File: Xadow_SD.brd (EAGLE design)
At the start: 25.5 x 20.4 mm, 6 parts, among them IC1 4050D, J1 MICRO-SDCARD-CONNECTOR-330006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, J2 12p FPC bottom contact, J3 12p FPC bottom contact

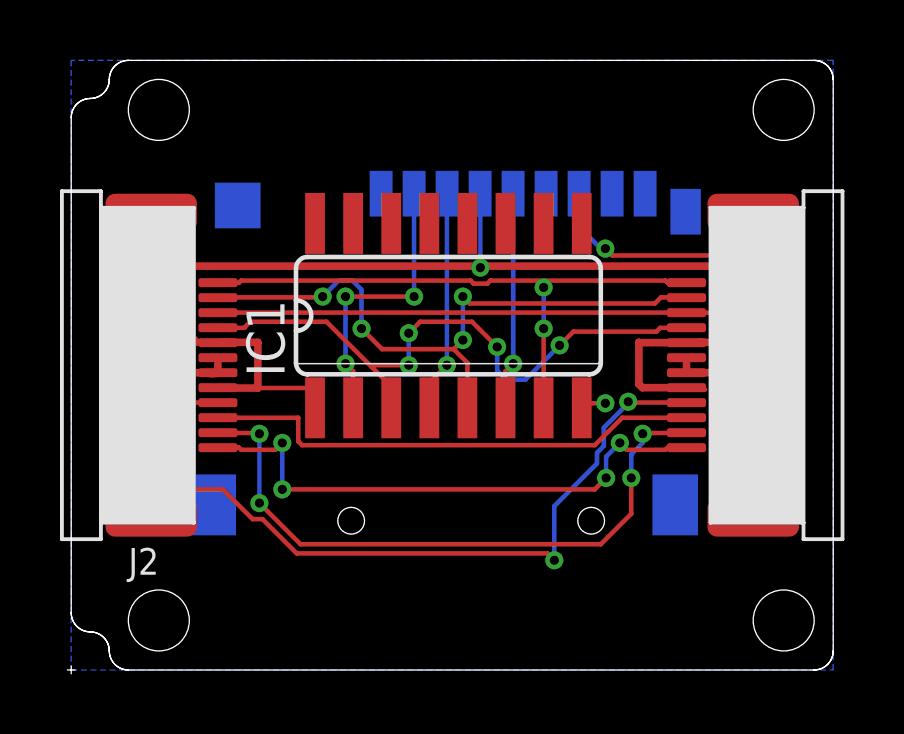
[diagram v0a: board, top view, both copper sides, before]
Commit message: Add 6-pin header
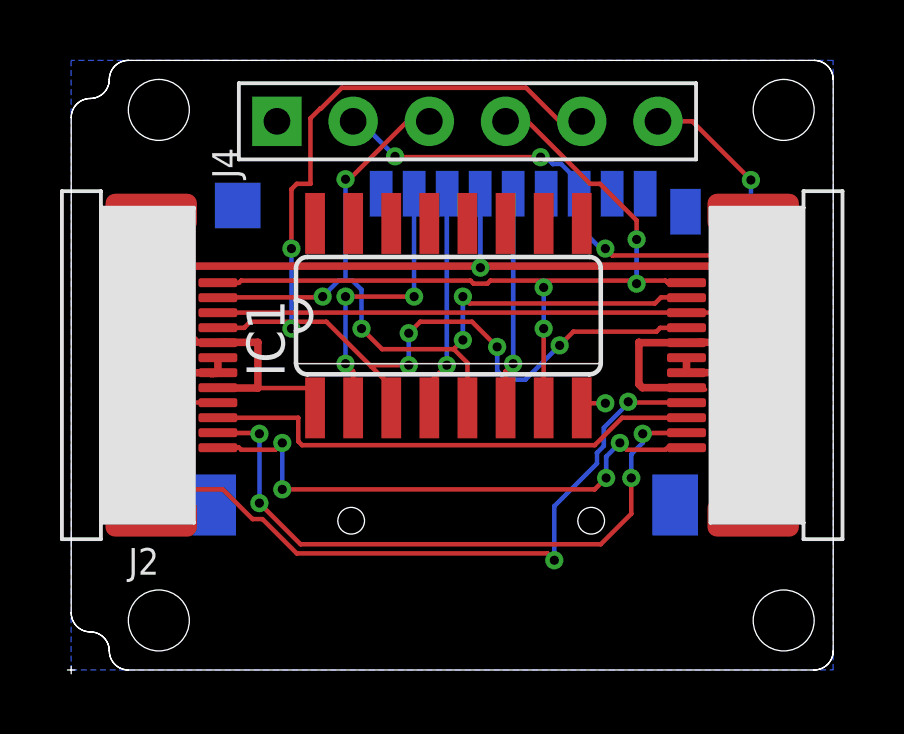
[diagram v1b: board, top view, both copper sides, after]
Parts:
- added J4: CONNECTOR-HEADER-6P-3460650P1, OPL:1X6P-2.54-2.54-11.6-3.0-BLACK-MALE
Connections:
- net 3V3: now also J4.6
- net GND: now also J1.G1, J1.G2, J1.G3, J1.G4, J4.1
- net PB1/D15/SCK: now also J4.4
- net PB2/D16/MOSI: now also J4.3
- net PB3/D14/MISO: now also J4.2
- net PF0/A5: now also J4.5
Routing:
- net PF0/A5: track 21.2 -> 38.9 mm, vias 4 -> 6
- net PB3/D14/MISO: track 25.0 -> 34.1 mm, vias 3 -> 5
- net PB1/D15/SCK: track 20.0 -> 28.0 mm, vias 2 -> 4
- net 3V3: track 42.2 -> 49.2 mm, vias 1 -> 3
- net PB2/D16/MOSI: track 21.5 -> 28.4 mm, vias 4 -> 5
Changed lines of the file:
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@@
 <layer number="18" name="Vias" color="2" fill="1" visible="yes" active="yes"/>
 <layer number="19" name="Unrouted" color="6" fill="1" visible="yes" active="yes"/>
-<layer number="20" name="Dimension" color="5" fill="1" visible="no" active="yes"/>
+<layer number="20" name="Dimension" color="5" fill="1" visible="yes" active="yes"/>
 <layer number="21" name="tPlace" color="7" fill="1" visible="no" active="yes"/>
 <layer number="22" name="bPlace" color="3" fill="1" visible="no" active="yes"/>
-<layer number="23" name="tOrigins" color="15" fill="1" visible="no" active="yes"/>
-<layer number="24" name="bOrigins" color="3" fill="1" visible="no" active="yes"/>
+<layer number="23" name="tOrigins" color="15" fill="1" visible="yes" active="yes"/>
+<layer number="24" name="bOrigins" color="3" fill="1" visible="yes" active="yes"/>
 <layer number="25" name="tNames" color="7" fill="1" visible="no" active="yes"/>
 <layer number="26" name="bNames" color="3" fill="1" visible="no" active="yes"/>
@@
 <element name="IC1" library="40xx" package="SO16" value="4050D" x="20.447" y="18.161"/>
 <element name="J1" library="OPL" package="9P-SMD-W-RING" value="MICRO-SDCARD-CONNECTOR-3300060P1" x="20.32" y="14.732" rot="MR270"/>
+<element name="J4" library="OPL" package="1X6P-2.54-2.54-11.6-3.0-BLACK-MALE" value="CONNECTOR-HEADER-6P-3460650P1" x="21.082" y="24.638" rot="R90"/>
 </elements>
 <signals>
@@
 <wire x1="12.7" y1="17.272" x2="12.764" y2="17.26" width="0.1524" layer="1"/>
 <via x="21.5138" y="19.7612" extent="1-16" drill="0.3048"/>
+<contactref element="J4" pad="6"/>
+<wire x1="28.575" y1="24.638" x2="27.432" y2="24.638" width="0.1524" layer="1"/>
+<wire x1="30.5308" y1="22.6822" x2="28.575" y2="24.638" width="0.1524" layer="1"/>
+<wire x1="30.5308" y1="20.3962" x2="30.5308" y2="22.6822" width="0.1524" layer="16"/>
+<wire x1="30.0482" y1="19.9136" x2="30.5308" y2="20.3962" width="0.1524" layer="1"/>
+<wire x1="30.0482" y1="19.9136" x2="29.972" y2="19.812" width="0.1524" layer="1"/>
+<via x="30.5308" y="22.6822" extent="1-16" drill="0.3048"/>
+<via x="30.5308" y="20.3962" extent="1-16" drill="0.3048"/>
 </signal>
 <signal name="GND">
@@
 <wire x1="12.764" y1="16.76" x2="12.764" y2="16.26" width="0.254" layer="1"/>
 <wire x1="12.4206" y1="16.256" x2="9.525" y2="16.256" width="0.254" layer="1"/>
+<contactref element="J4" pad="1"/>
+<contactref element="J1" pad="G3"/>
+<contactref element="J1" pad="G2"/>
+<contactref element="J1" pad="G1"/>
+<contactref element="J1" pad="G4"/>
 </signal>
 <signal name="PB1/D15/SCK">
@@
 <wire x1="21.7424" y1="19.2278" x2="21.2852" y2="19.2278" width="0.1524" layer="1"/>
 <wire x1="21.844" y1="19.3294" x2="21.7424" y2="19.2278" width="0.1524" layer="1"/>
-<wire x1="27.686" y1="19.3294" x2="23.622" y2="19.3294" width="0.1524" layer="1"/>
+<wire x1="27.686" y1="19.3294" x2="26.7208" y2="19.3294" width="0.1524" layer="1"/>
+<wire x1="26.7208" y1="19.3294" x2="23.622" y2="19.3294" width="0.1524" layer="1"/>
 <wire x1="23.622" y1="19.3294" x2="21.844" y2="19.3294" width="0.1524" layer="1"/>
 <wire x1="27.7622" y1="19.2532" x2="27.686" y2="19.3294" width="0.1524" layer="1"/>
@@
 <via x="23.622" y="17.7292" extent="1-16" drill="0.3048"/>
 <via x="23.622" y="19.1008" extent="1-16" drill="0.3048"/>
+<contactref element="J4" pad="4"/>
+<wire x1="23.0886" y1="24.638" x2="22.352" y2="24.638" width="0.1524" layer="1"/>
+<wire x1="25.1714" y1="22.5552" x2="23.0886" y2="24.638" width="0.1524" layer="1"/>
+<wire x1="25.5016" y1="22.5552" x2="25.1714" y2="22.5552" width="0.1524" layer="1"/>
+<wire x1="26.7208" y1="21.336" x2="25.5016" y2="22.5552" width="0.1524" layer="1"/>
+<wire x1="26.7208" y1="20.701" x2="26.7208" y2="21.336" width="0.1524" layer="1"/>
+<wire x1="26.7208" y1="19.2278" x2="26.7208" y2="20.701" width="0.1524" layer="16"/>
+<wire x1="26.7208" y1="19.2278" x2="26.7208" y2="19.3294" width="0.1524" layer="1"/>
+<via x="26.7208" y="20.701" extent="1-16" drill="0.3048"/>
+<via x="26.7208" y="19.2278" extent="1-16" drill="0.3048"/>
 </signal>
 <signal name="PB3/D14/MISO">
@@
 <via x="29.5148" y="20.3962" extent="1-16" drill="0.3048"/>
 <via x="29.5148" y="18.5166" extent="1-16" drill="0.3048"/>
+<contactref element="J4" pad="2"/>
+<wire x1="17.272" y1="24.3078" x2="17.272" y2="24.638" width="0.1524" layer="16"/>
+<wire x1="17.3482" y1="24.2316" x2="17.272" y2="24.3078" width="0.1524" layer="16"/>
+<wire x1="17.907" y1="24.2316" x2="17.3482" y2="24.2316" width="0.1524" layer="16"/>
+<wire x1="18.669" y1="23.4696" x2="17.907" y2="24.2316" width="0.1524" layer="16"/>
+<wire x1="18.6944" y1="23.4442" x2="18.669" y2="23.4696" width="0.1524" layer="1"/>
+<wire x1="23.5204" y1="23.4442" x2="18.6944" y2="23.4442" width="0.1524" layer="1"/>
+<wire x1="23.6982" y1="23.4442" x2="23.5204" y2="23.4442" width="0.1524" layer="16"/>
+<wire x1="23.9268" y1="23.2156" x2="23.6982" y2="23.4442" width="0.1524" layer="16"/>
+<wire x1="24.2062" y1="23.2156" x2="23.9268" y2="23.2156" width="0.1524" layer="16"/>
+<wire x1="24.638" y1="22.7838" x2="24.2062" y2="23.2156" width="0.1524" layer="16"/>
+<wire x1="24.8158" y1="22.7838" x2="24.638" y2="22.7838" width="0.1524" layer="16"/>
+<wire x1="24.8158" y1="22.2758" x2="24.8158" y2="22.7838" width="0.1524" layer="16"/>
+<wire x1="24.8158" y1="22.2758" x2="24.806" y2="22.225" width="0.1524" layer="16"/>
+<via x="18.669" y="23.4696" extent="1-16" drill="0.3048"/>
+<via x="23.5204" y="23.4442" extent="1-16" drill="0.3048"/>
 </signal>
 <signal name="PB2/D16/MOSI">
@@
 <wire x1="16.256" y1="18.796" x2="16.2306" y2="18.7706" width="0.1524" layer="1"/>
 <wire x1="16.7894" y1="19.3294" x2="16.256" y2="18.796" width="0.1524" layer="16"/>
-<wire x1="17.2466" y1="19.3294" x2="16.7894" y2="19.3294" width="0.1524" layer="16"/>
+<wire x1="17.2466" y1="19.3294" x2="17.018" y2="19.3294" width="0.1524" layer="16"/>
+<wire x1="17.018" y1="19.3294" x2="16.7894" y2="19.3294" width="0.1524" layer="16"/>
 <wire x1="17.5514" y1="19.0246" x2="17.2466" y2="19.3294" width="0.1524" layer="16"/>
 <wire x1="17.5514" y1="17.7292" x2="17.5514" y2="19.0246" width="0.1524" layer="16"/>
@@
 <via x="20.9296" y="18.796" extent="1-16" drill="0.3048"/>
 <via x="20.9296" y="17.3482" extent="1-16" drill="0.3048"/>
+<contactref element="J4" pad="3"/>
+<wire x1="19.0754" y1="24.638" x2="19.812" y2="24.638" width="0.1524" layer="1"/>
+<wire x1="17.145" y1="22.7076" x2="19.0754" y2="24.638" width="0.1524" layer="1"/>
+<wire x1="17.018" y1="22.7076" x2="17.145" y2="22.7076" width="0.1524" layer="1"/>
+<wire x1="17.018" y1="19.3294" x2="17.018" y2="22.7076" width="0.1524" layer="16"/>
+<via x="17.018" y="22.7076" extent="1-16" drill="0.3048"/>
 </signal>
 <signal name="PD3/TXO/D1">
@@
 <wire x1="13.6398" y1="17.7546" x2="12.8524" y2="17.7546" width="0.1524" layer="1"/>
 <wire x1="13.843" y1="17.9578" x2="13.6398" y2="17.7546" width="0.1524" layer="1"/>
-<wire x1="16.383" y1="17.9578" x2="13.843" y2="17.9578" width="0.1524" layer="1"/>
+<wire x1="16.383" y1="17.9578" x2="15.2146" y2="17.9578" width="0.1524" layer="1"/>
+<wire x1="15.2146" y1="17.9578" x2="13.843" y2="17.9578" width="0.1524" layer="1"/>
 <wire x1="18.542" y1="15.7988" x2="17.8816" y2="16.4592" width="0.1524" layer="1"/>
 <wire x1="17.8816" y1="16.4592" x2="16.383" y2="17.9578" width="0.1524" layer="1"/>
@@
 <via x="19.1262" y="17.5768" extent="1-16" drill="0.3048"/>
 <via x="19.1262" y="16.51" extent="1-16" drill="0.3048"/>
+<contactref element="J4" pad="5"/>
+<wire x1="24.1554" y1="24.638" x2="24.892" y2="24.638" width="0.1524" layer="1"/>
+<wire x1="23.0378" y1="25.7556" x2="24.1554" y2="24.638" width="0.1524" layer="1"/>
+<wire x1="16.891" y1="25.7556" x2="23.0378" y2="25.7556" width="0.1524" layer="1"/>
+<wire x1="16.2052" y1="25.0698" x2="16.891" y2="25.7556" width="0.1524" layer="1"/>
+<wire x1="16.1798" y1="25.0698" x2="16.2052" y2="25.0698" width="0.1524" layer="1"/>
+<wire x1="15.8496" y1="24.7396" x2="16.1798" y2="25.0698" width="0.1524" layer="1"/>
+<wire x1="15.8496" y1="22.5552" x2="15.8496" y2="24.7396" width="0.1524" layer="1"/>
+<wire x1="15.3924" y1="22.5552" x2="15.8496" y2="22.5552" width="0.1524" layer="1"/>
+<wire x1="15.2146" y1="22.3774" x2="15.3924" y2="22.5552" width="0.1524" layer="1"/>
+<wire x1="15.2146" y1="20.3962" x2="15.2146" y2="22.3774" width="0.1524" layer="1"/>
+<wire x1="15.2146" y1="17.7292" x2="15.2146" y2="20.3962" width="0.1524" layer="16"/>
+<wire x1="15.2146" y1="17.9578" x2="15.2146" y2="17.7292" width="0.1524" layer="1"/>
+<via x="15.2146" y="20.3962" extent="1-16" drill="0.3048"/>
+<via x="15.2146" y="17.7292" extent="1-16" drill="0.3048"/>
 </signal>
 <signal name="PD1/SDA/D2">

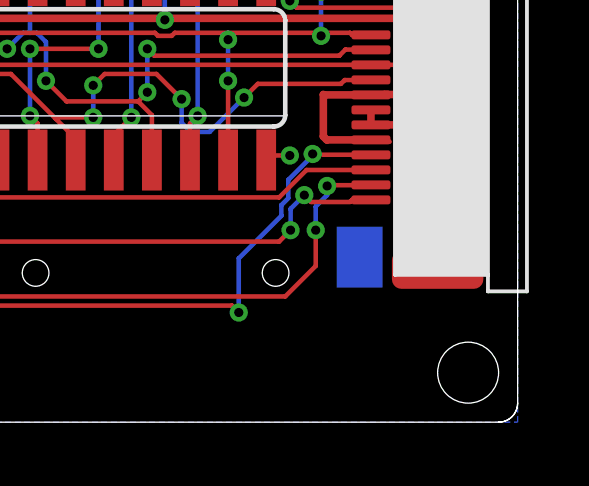
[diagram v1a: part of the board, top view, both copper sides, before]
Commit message: Add labels and move graphics
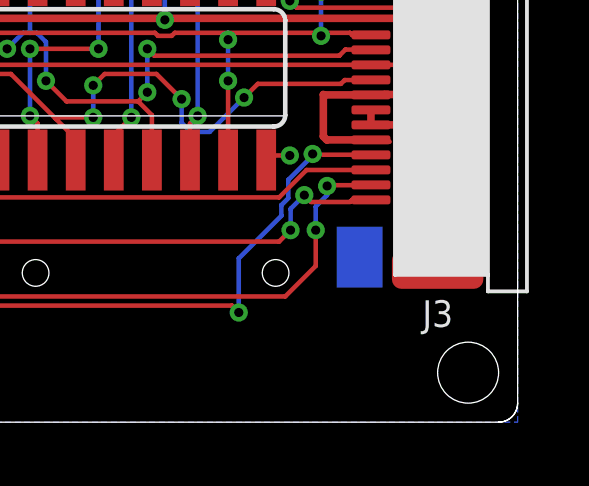
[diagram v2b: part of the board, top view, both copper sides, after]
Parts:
- moved U$2 15.4 mm to (31.1, 12.7), turned to 270 degrees
- moved U$3 7.94 mm to (33.0, 22.9), turned to 270 degrees
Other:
- board text added: "3V3"
- board text added: "CS"
- board text added: "GND"
- board text added: "MISO"
- board text added: "MOSI"
- board text added: "SCK"
- board text added: "by Tisham Dhar"
- board text added: "v2.0 02/09/2014"
- board text removed: "by Seeed Studio"
- board text removed: "v1.0 06/08/2014"
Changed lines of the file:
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@@
 <layer number="19" name="Unrouted" color="6" fill="1" visible="yes" active="yes"/>
 <layer number="20" name="Dimension" color="5" fill="1" visible="yes" active="yes"/>
-<layer number="21" name="tPlace" color="7" fill="1" visible="no" active="yes"/>
-<layer number="22" name="bPlace" color="3" fill="1" visible="no" active="yes"/>
+<layer number="21" name="tPlace" color="7" fill="1" visible="yes" active="yes"/>
+<layer number="22" name="bPlace" color="3" fill="1" visible="yes" active="yes"/>
 <layer number="23" name="tOrigins" color="15" fill="1" visible="yes" active="yes"/>
 <layer number="24" name="bOrigins" color="3" fill="1" visible="yes" active="yes"/>
-<layer number="25" name="tNames" color="7" fill="1" visible="no" active="yes"/>
-<layer number="26" name="bNames" color="3" fill="1" visible="no" active="yes"/>
-<layer number="27" name="tValues" color="7" fill="1" visible="no" active="yes"/>
-<layer number="28" name="bValues" color="7" fill="1" visible="no" active="yes"/>
-<layer number="29" name="tStop" color="7" fill="3" visible="no" active="yes"/>
-<layer number="30" name="bStop" color="3" fill="6" visible="no" active="yes"/>
-<layer number="31" name="tCream" color="7" fill="4" visible="no" active="yes"/>
-<layer number="32" name="bCream" color="3" fill="5" visible="no" active="yes"/>
-<layer number="33" name="tFinish" color="6" fill="3" visible="no" active="yes"/>
-<layer number="34" name="bFinish" color="3" fill="6" visible="no" active="yes"/>
-<layer number="35" name="tGlue" color="7" fill="4" visible="no" active="yes"/>
-<layer number="36" name="bGlue" color="3" fill="5" visible="no" active="yes"/>
-<layer number="37" name="tTest" color="7" fill="1" visible="no" active="yes"/>
-<layer number="38" name="bTest" color="3" fill="1" visible="no" active="yes"/>
-<layer number="39" name="tKeepout" color="4" fill="11" visible="no" active="yes"/>
-<layer number="40" name="bKeepout" color="1" fill="11" visible="no" active="yes"/>
-<layer number="41" name="tRestrict" color="4" fill="10" visible="no" active="yes"/>
-<layer number="42" name="bRestrict" color="1" fill="10" visible="no" active="yes"/>
-<layer number="43" name="vRestrict" color="2" fill="10" visible="no" active="yes"/>
-<layer number="44" name="Drills" color="7" fill="1" visible="no" active="yes"/>
-<layer number="45" name="Holes" color="7" fill="1" visible="no" active="yes"/>
-<layer number="46" name="Milling" color="3" fill="1" visible="no" active="yes"/>
-<layer number="47" name="Measures" color="7" fill="1" visible="no" active="yes"/>
-<layer number="48" name="Document" color="7" fill="1" visible="no" active="yes"/>
-<layer number="49" name="Reference" color="7" fill="1" visible="no" active="yes"/>
-<layer number="50" name="dxf" color="7" fill="1" visible="no" active="yes"/>
-<layer number="51" name="tDocu" color="7" fill="1" visible="no" active="yes"/>
-<layer number="52" name="bDocu" color="7" fill="1" visible="no" active="yes"/>
+<layer number="25" name="tNames" color="7" fill="1" visible="yes" active="yes"/>
+<layer number="26" name="bNames" color="3" fill="1" visible="yes" active="yes"/>
+<layer number="27" name="tValues" color="7" fill="1" visible="yes" active="yes"/>
+<layer number="28" name="bValues" color="7" fill="1" visible="yes" active="yes"/>
+<layer number="29" name="tStop" color="7" fill="3" visible="yes" active="yes"/>
+<layer number="30" name="bStop" color="3" fill="6" visible="yes" active="yes"/>
+<layer number="31" name="tCream" color="7" fill="4" visible="yes" active="yes"/>
+<layer number="32" name="bCream" color="3" fill="5" visible="yes" active="yes"/>
+<layer number="33" name="tFinish" color="6" fill="3" visible="yes" active="yes"/>
+<layer number="34" name="bFinish" color="3" fill="6" visible="yes" active="yes"/>
+<layer number="35" name="tGlue" color="7" fill="4" visible="yes" active="yes"/>
+<layer number="36" name="bGlue" color="3" fill="5" visible="yes" active="yes"/>
+<layer number="37" name="tTest" color="7" fill="1" visible="yes" active="yes"/>
+<layer number="38" name="bTest" color="3" fill="1" visible="yes" active="yes"/>
+<layer number="39" name="tKeepout" color="4" fill="11" visible="yes" active="yes"/>
+<layer number="40" name="bKeepout" color="1" fill="11" visible="yes" active="yes"/>
+<layer number="41" name="tRestrict" color="4" fill="10" visible="yes" active="yes"/>
+<layer number="42" name="bRestrict" color="1" fill="10" visible="yes" active="yes"/>
+<layer number="43" name="vRestrict" color="2" fill="10" visible="yes" active="yes"/>
+<layer number="44" name="Drills" color="7" fill="1" visible="yes" active="yes"/>
+<layer number="45" name="Holes" color="7" fill="1" visible="yes" active="yes"/>
+<layer number="46" name="Milling" color="3" fill="1" visible="yes" active="yes"/>
+<layer number="47" name="Measures" color="7" fill="1" visible="yes" active="yes"/>
+<layer number="48" name="Document" color="7" fill="1" visible="yes" active="yes"/>
+<layer number="49" name="Reference" color="7" fill="1" visible="yes" active="yes"/>
+<layer number="50" name="dxf" color="7" fill="1" visible="yes" active="yes"/>
+<layer number="51" name="tDocu" color="7" fill="1" visible="yes" active="yes"/>
+<layer number="52" name="bDocu" color="7" fill="1" visible="yes" active="yes"/>
 <layer number="91" name="Nets" color="2" fill="1" visible="no" active="no"/>
 <layer number="92" name="Busses" color="1" fill="1" visible="no" active="no"/>
@@
 <layer number="111" name="111" color="7" fill="1" visible="no" active="no"/>
 <layer number="112" name="tSilk" color="7" fill="1" visible="no" active="no"/>
-<layer number="116" name="Patch_BOT" color="9" fill="4" visible="no" active="yes"/>
+<layer number="116" name="Patch_BOT" color="9" fill="4" visible="yes" active="yes"/>
 <layer number="118" name="Rect_Pads" color="7" fill="1" visible="no" active="no"/>
 <layer number="121" name="_tsilk" color="7" fill="1" visible="no" active="no"/>
@@
 <rectangle x1="28.067" y1="16.256" x2="28.702" y2="16.764" layer="41"/>
 <rectangle x1="12.573" y1="16.256" x2="13.081" y2="16.764" layer="41"/>
-<text x="26.924" y="15.875" size="1.27" layer="22" ratio="12" rot="MR0">Xadow SD</text>
+<text x="12.446" y="21.209" size="1.016" layer="22" ratio="12" rot="MR270">Xadow SD</text>
 <text x="5.969" y="-1.397" size="1.27" layer="22" ratio="12" rot="MR0"></text>
-<text x="26.924" y="14.605" size="0.889" layer="22" ratio="11" rot="MR0">v1.0 06/08/2014</text>
-<text x="26.924" y="13.335" size="0.889" layer="22" ratio="11" rot="MR0">by Seeed Studio</text>
+<text x="9.271" y="22.733" size="0.889" layer="22" ratio="11" rot="MR270">v2.0 02/09/2014</text>
+<text x="10.795" y="22.606" size="0.889" layer="22" ratio="11" rot="MR270">by Tisham Dhar</text>
 <wire x1="33.274" y1="6.985" x2="33.274" y2="26.035" width="0.0254" layer="20"/>
 <wire x1="33.274" y1="26.035" x2="32.639" y2="26.67" width="0.0254" layer="20" curve="90"/>
@@
 <wire x1="7.747" y1="6.35" x2="8.001" y2="6.35" width="0" layer="20"/>
 <wire x1="7.874" y1="6.477" x2="7.874" y2="6.223" width="0" layer="20"/>
+<text x="13.335" y="25.908" size="0.6096" layer="22" ratio="12" rot="MR270">GND</text>
+<text x="29.464" y="26.162" size="0.6096" layer="22" font="vector" ratio="12" rot="MR270">3V3</text>
+<text x="17.78" y="23.241" size="0.4064" layer="22" ratio="12" rot="MR0">MISO</text>
+<text x="20.574" y="23.241" size="0.4064" layer="22" ratio="12" rot="MR0">MOSI</text>
+<text x="22.86" y="23.241" size="0.4064" layer="22" ratio="12" rot="MR0">SCK</text>
+<text x="25.273" y="23.241" size="0.4064" layer="22" ratio="12" rot="MR0">CS</text>
 </plain>
 <attributes>
@@
 </element>
 <element name="J3" library="template" package="12P-0.5" value="12p FPC bottom contact" x="30.734" y="16.51" smashed="yes" rot="R90">
-<attribute name="NAME" x="30.099" y="9.525" size="0.889" layer="26" ratio="11" rot="MR0"/>
+<attribute name="NAME" x="30.099" y="9.525" size="0.889" layer="25" ratio="11"/>
 <attribute name="VALUE" x="34.719" y="14.617" size="0.889" layer="27" ratio="11" rot="R90"/>
 </element>
-<element name="U$2" library="Logo" package="LOGO_SILK" value="" x="17.399" y="19.685" rot="MR0"/>
-<element name="U$3" library="Logo" package="OSHW_FILLX200_NOTEXT" value="" x="26.924" y="17.78" rot="MR0"/>
+<element name="U$2" library="Logo" package="LOGO_SILK" value="" x="31.115" y="12.7" rot="MR270"/>
+<element name="U$3" library="Logo" package="OSHW_FILLX200_NOTEXT" value="" x="33.02" y="22.86" rot="MR270"/>
 <element name="IC1" library="40xx" package="SO16" value="4050D" x="20.447" y="18.161"/>
 <element name="J1" library="OPL" package="9P-SMD-W-RING" value="MICRO-SDCARD-CONNECTOR-3300060P1" x="20.32" y="14.732" rot="MR270"/>
@@
 </signal>
 </signals>
-<errors>
-</errors>
 </board>
 </drawing>
